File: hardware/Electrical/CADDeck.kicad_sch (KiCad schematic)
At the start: 46 parts, among them J1 Conn_01x05_Socket, J2 Conn_01x05_Pin, J3 Conn_01x04_Pin, J4 Conn_01x04_Socket, J5 Conn_01x10_Socket, J6 Conn_01x10_Pin, Q1 2N2222, SW1 SW_Push, SW10 SW_Push, SW2 SW_Push, SW3 SW_Push, SW4 SW_Push, SW5 SW_Push, SW6 SW_Push, SW7 SW_Push, SW8 SW_Push, SW9 SW_Push, U1 PCF8575PWE4, U3 TTP223, U5 49E Rotate, U6 49E Zoom

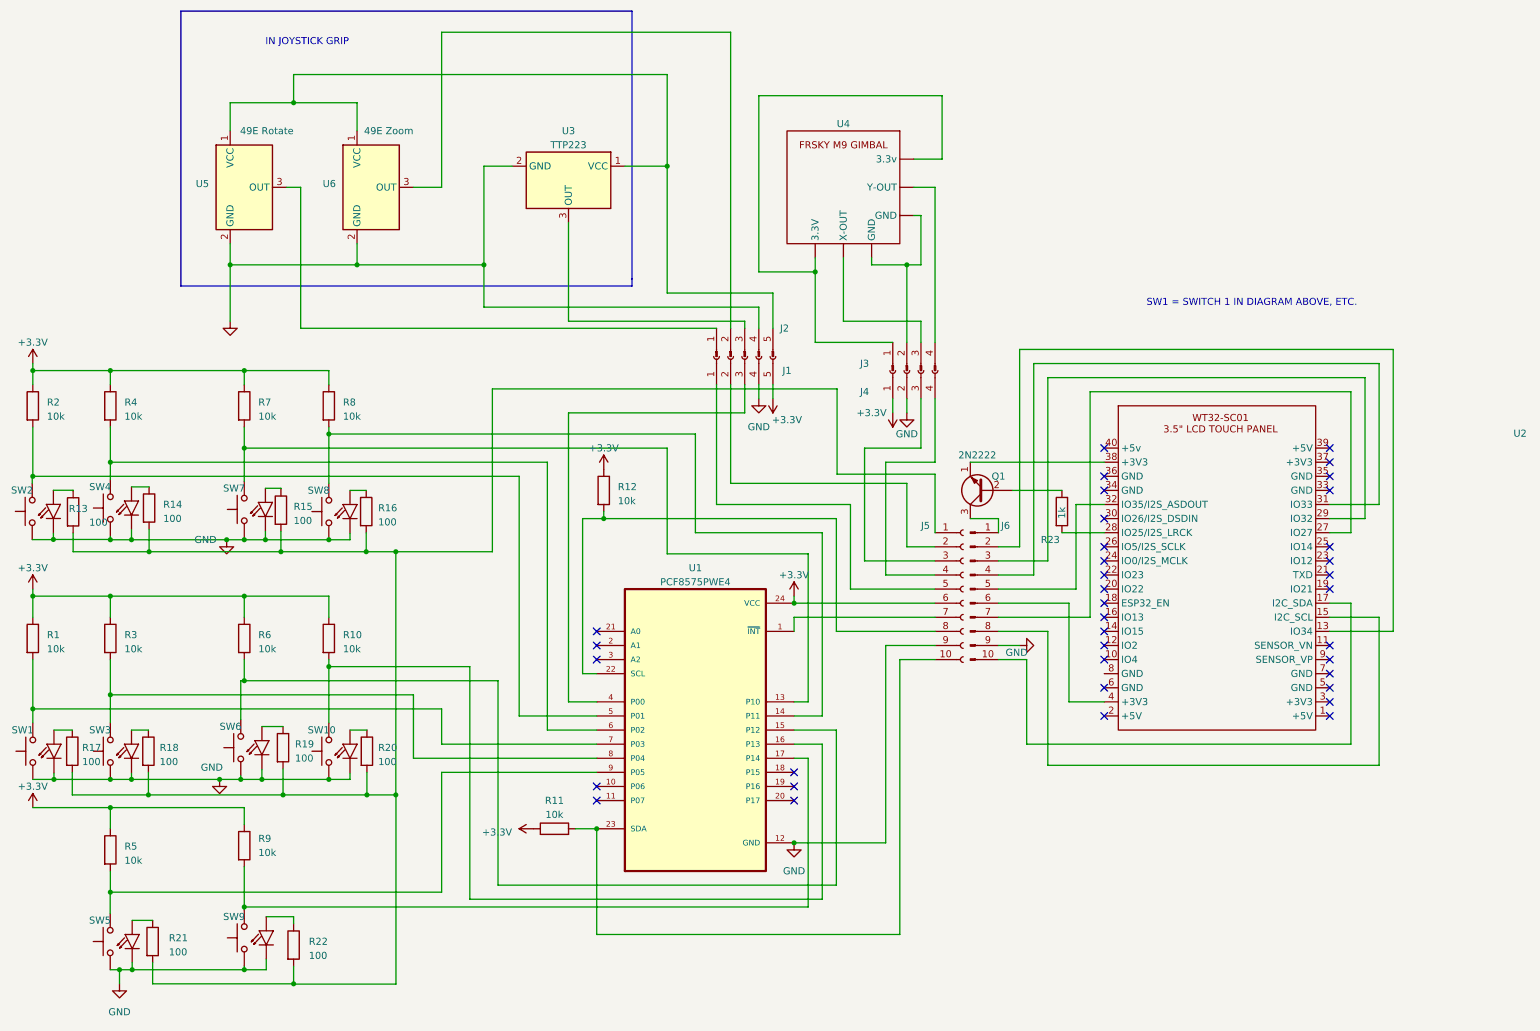
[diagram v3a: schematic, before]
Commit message: Board Transistor eingefügt
Für LED Beleuchtung und Leiterbahnen angepasst.
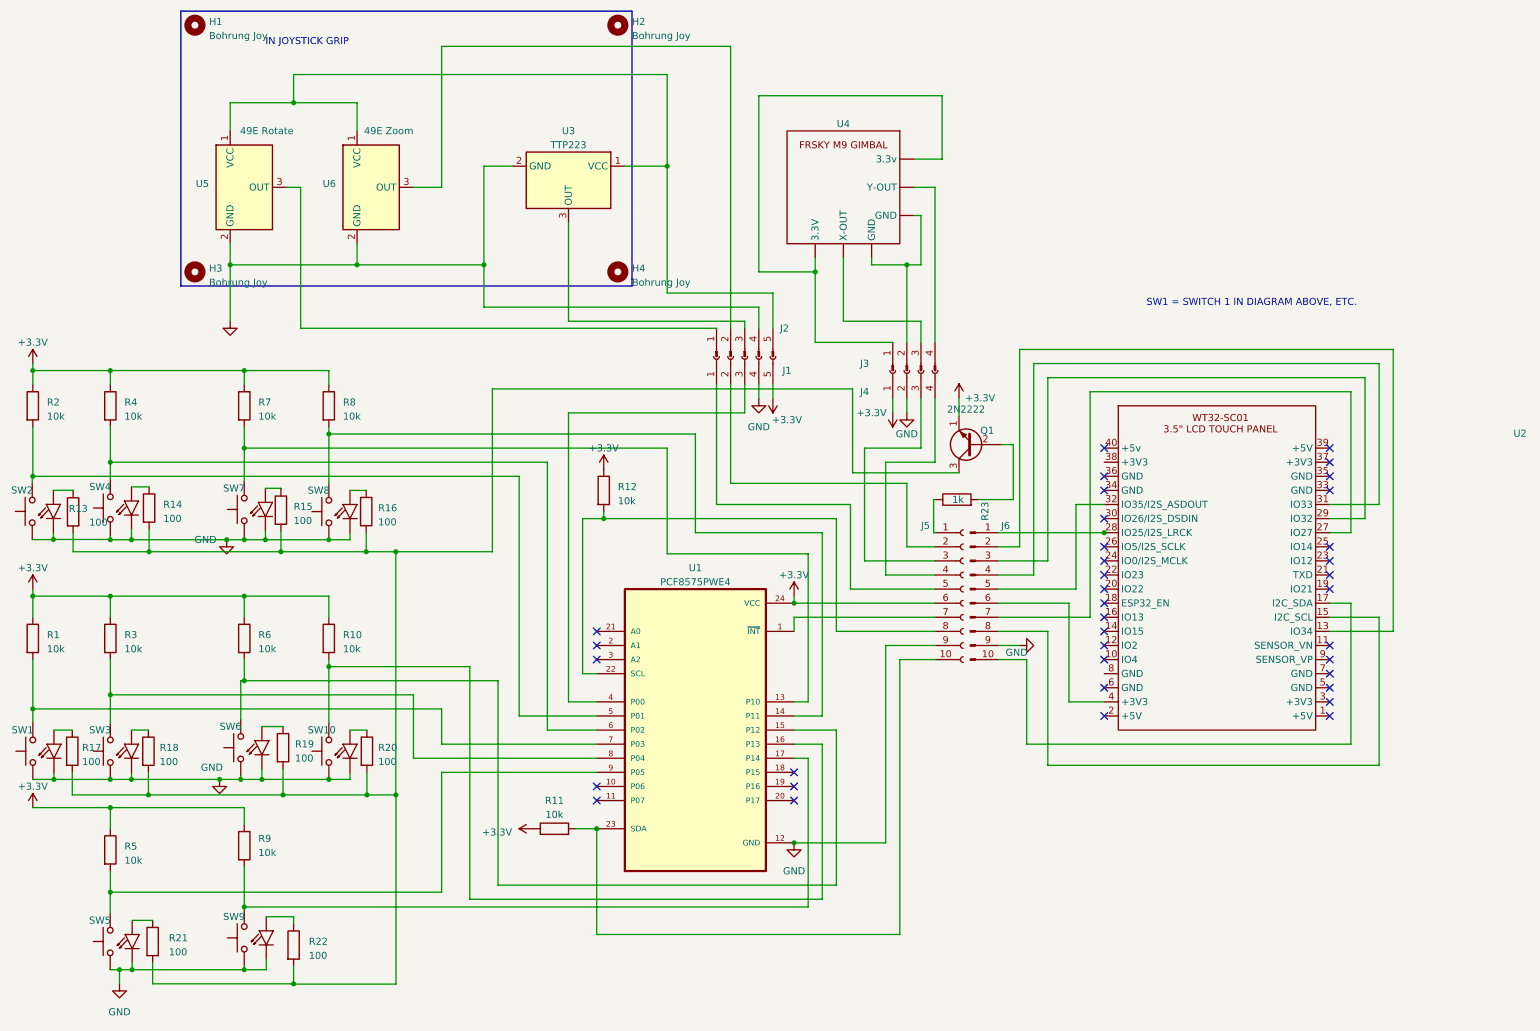
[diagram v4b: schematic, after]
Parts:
- added H1, H2, H3, H4: Bohrung Joy, MountingHole:MountingHole_3.2mm_M3_DIN965, symbol Mechanical:MountingHole
- Q1: footprint Package_TO_SOT_THT:TO-39-3 -> Package_TO_SOT_SMD:TSOT-23
- R23: footprint (none) -> Resistor_SMD:R_0805_2012Metric_Pad1.20x1.40mm_HandSolder
- U3: footprint (none) -> Package_TO_SOT_SMD:TSOT-23
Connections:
- net +3.3V: now also Q1.1 (E)
- net at U2.38 (+3V3): no longer Q1.1 (E)
- net at Q1.2 (B): now also R23.2; no longer R23.1
- net at Q1.3 (C): now also R13.2, R14.2, R15.2, R16.2, R17.2, R18.2, R19.2, R20.2, R21.2, R22.2; no longer J6.1 (Pin_1)
- net at U2.28 (IO25/I2S_LRCK): now also J6.1 (Pin_1); no longer R23.2
- new net: J5.1 (Pin_1), R23.1
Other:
- moved on the sheet: Q1, R23

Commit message: Neue Platine in 3D Modell eingefügt
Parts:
- J1: footprint Connector_JST:JST_EH_B5B-EH-A_1x05_P2.50mm_Vertical -> Connector_JST:JST_EH_S5B-EH_1x05_P2.50mm_Horizontal
- J4: footprint Connector_JST:JST_EH_B4B-EH-A_1x04_P2.50mm_Vertical -> Connector_JST:JST_EH_S4B-EH_1x04_P2.50mm_Horizontal
- J5: footprint Connector_JST:JST_EH_B10B-EH-A_1x10_P2.50mm_Vertical -> Connector_JST:JST_EH_S10B-EH_1x10_P2.50mm_Horizontal
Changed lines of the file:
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@@
       (effects (font (size 1.27 1.27)) hide)
     )
-    (property "Footprint" "Connector_JST:JST_EH_B5B-EH-A_1x05_P2.50mm_Vertical" (at 144.78 78.74 0)
+    (property "Footprint" "Connector_JST:JST_EH_S5B-EH_1x05_P2.50mm_Horizontal" (at 144.78 78.74 0)
       (effects (font (size 1.27 1.27)) hide)
     )
@@
       (effects (font (size 1.27 1.27)) hide)
     )
-    (property "Footprint" "Connector_JST:JST_EH_B4B-EH-A_1x04_P2.50mm_Vertical" (at 173.99 81.28 0)
+    (property "Footprint" "Connector_JST:JST_EH_S4B-EH_1x04_P2.50mm_Horizontal" (at 173.99 81.28 0)
       (effects (font (size 1.27 1.27)) hide)
     )
@@
       (effects (font (size 1.27 1.27)) (justify left) hide)
     )
-    (property "Footprint" "Connector_JST:JST_EH_B10B-EH-A_1x10_P2.50mm_Vertical" (at 184.15 120.65 0)
-      (effects (font (size 1.27 1.27)) hide)
-    )
+    (property "Footprint" "Connector_JST:JST_EH_S10B-EH_1x10_P2.50mm_Horizontal" (at 184.15 120.65 0)
+      (effects (font (size 1.27 1.27)) hide)
+    )

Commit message: Kleine Korrekturen
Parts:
- removed H1, H2, H3, H4: Bohrung Joy, MountingHole:MountingHole_3.2mm_M3_DIN965, symbol Mechanical:MountingHole
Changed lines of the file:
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@@
-    )
-  )
-  (symbol (lib_id "Mechanical:MountingHole") (at 45.72 19.05 0) (unit 1)
-    (in_bom yes) (on_board yes) (dnp no) (fields_autoplaced)
-    (property "Reference" "H1" (at 48.26 18.415 0)
-      (effects (font (size 1.27 1.27)) (justify left))
-    )
-    (property "Value" "Bohrung Joy" (at 48.26 20.955 0)
-      (effects (font (size 1.27 1.27)) (justify left))
-    )
-    (property "Footprint" "MountingHole:MountingHole_3.2mm_M3_DIN965" (at 45.72 19.05 0)
-      (effects (font (size 1.27 1.27)) hide)
-    )
-    (property "Datasheet" "~" (at 45.72 19.05 0)
-      (effects (font (size 1.27 1.27)) hide)
-    )
-    (instances
-      (project "CADDeck"
-        (path "/35ea3785-d2ac-411c-b2c0-fb3fbf77b703"
-          (reference "H1") (unit 1)
-        )
-      )
     )
   )
@@
         (path "/35ea3785-d2ac-411c-b2c0-fb3fbf77b703"
           (reference "R13") (unit 1)
-        )
-      )
-    )
-  )
-  (symbol (lib_id "Mechanical:MountingHole") (at 121.92 19.05 0) (unit 1)
-    (in_bom yes) (on_board yes) (dnp no) (fields_autoplaced)
-    (property "Reference" "H2" (at 124.46 18.415 0)
-      (effects (font (size 1.27 1.27)) (justify left))
-    )
-    (property "Value" "Bohrung Joy" (at 124.46 20.955 0)
-      (effects (font (size 1.27 1.27)) (justify left))
-    )
-    (property "Footprint" "MountingHole:MountingHole_3.2mm_M3_DIN965" (at 121.92 19.05 0)
-      (effects (font (size 1.27 1.27)) hide)
-    )
-    (property "Datasheet" "~" (at 121.92 19.05 0)
-      (effects (font (size 1.27 1.27)) hide)
-    )
-    (instances
-      (project "CADDeck"
-        (path "/35ea3785-d2ac-411c-b2c0-fb3fbf77b703"
-          (reference "H2") (unit 1)
         )
       )
@@
         (path "/35ea3785-d2ac-411c-b2c0-fb3fbf77b703"
           (reference "#PWR07") (unit 1)
-        )
-      )
-    )
-  )
-  (symbol (lib_id "Mechanical:MountingHole") (at 121.92 63.5 0) (unit 1)
-    (in_bom yes) (on_board yes) (dnp no) (fields_autoplaced)
-    (property "Reference" "H4" (at 124.46 62.865 0)
-      (effects (font (size 1.27 1.27)) (justify left))
-    )
-    (property "Value" "Bohrung Joy" (at 124.46 65.405 0)
-      (effects (font (size 1.27 1.27)) (justify left))
-    )
-    (property "Footprint" "MountingHole:MountingHole_3.2mm_M3_DIN965" (at 121.92 63.5 0)
-      (effects (font (size 1.27 1.27)) hide)
-    )
-    (property "Datasheet" "~" (at 121.92 63.5 0)
-      (effects (font (size 1.27 1.27)) hide)
-    )
-    (instances
-      (project "CADDeck"
-        (path "/35ea3785-d2ac-411c-b2c0-fb3fbf77b703"
-          (reference "H4") (unit 1)
         )
       )
@@
         )
       )
-    )
-  )
-  (symbol (lib_id "Mechanical:MountingHole") (at 45.72 63.5 0) (unit 1)
-    (in_bom yes) (on_board yes) (dnp no) (fields_autoplaced)
-    (property "Reference" "H3" (at 48.26 62.865 0)
-      (effects (font (size 1.27 1.27)) (justify left))
-    )
-    (property "Value" "Bohrung Joy" (at 48.26 65.405 0)
-      (effects (font (size 1.27 1.27)) (justify left))
-    )
-    (property "Footprint" "MountingHole:MountingHole_3.2mm_M3_DIN965" (at 45.72 63.5 0)
-      (effects (font (size 1.27 1.27)) hide)
-    )
-    (property "Datasheet" "~" (at 45.72 63.5 0)
-      (effects (font (size 1.27 1.27)) hide)
-    )
-    (instances
-      (project "CADDeck"
-        (path "/35ea3785-d2ac-411c-b2c0-fb3fbf77b703"
-          (reference "H3") (unit 1)
-        )
-      )

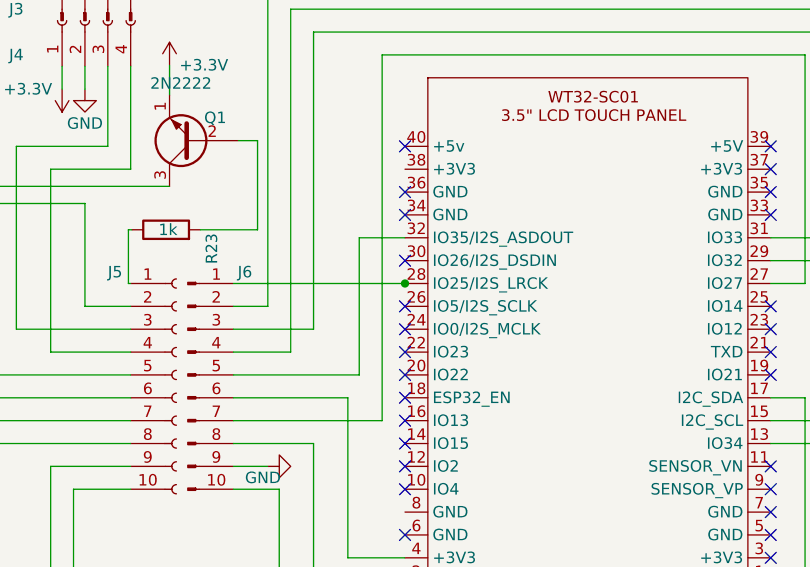
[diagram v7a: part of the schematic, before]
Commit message: Footprints geändert
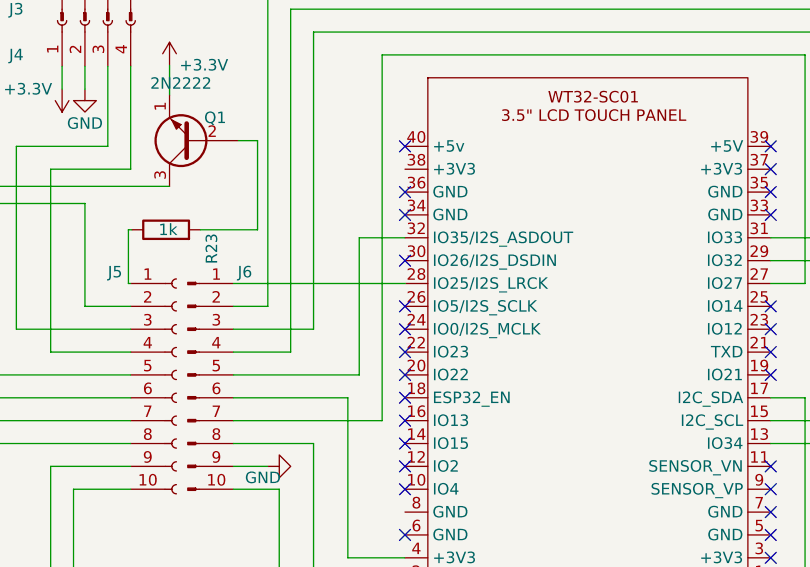
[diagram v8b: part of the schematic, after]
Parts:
- J1: footprint Connector_JST:JST_EH_S5B-EH_1x05_P2.50mm_Horizontal -> Connector_JST:JST_EH_B5B-EH-A_1x05_P2.50mm_Vertical
- J4: footprint Connector_JST:JST_EH_S4B-EH_1x04_P2.50mm_Horizontal -> Connector_JST:JST_EH_B4B-EH-A_1x04_P2.50mm_Vertical
- J5: footprint Connector_JST:JST_EH_S10B-EH_1x10_P2.50mm_Horizontal -> Connector_JST:JST_EH_B10B-EH-A_1x10_P2.50mm_Vertical
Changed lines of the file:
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@@
   (junction (at 54.61 111.76) (diameter 0) (color 0 0 0 0)
   )
-  (junction (at 209.55 110.49) (diameter 0) (color 0 0 0 0)
-  )
   (junction (at 16.51 142.24) (diameter 0) (color 0 0 0 0)
   )
@@
     (stroke (width 0) (type default))
   )
+  (wire (pts (xy 190.5 110.49) (xy 209.55 110.49))
+    (stroke (width 0) (type default))
+  )
   (wire (pts (xy 34.29 154.94) (xy 50.165 154.94))
     (stroke (width 0) (type default))
@@
     (stroke (width 0) (type default))
   )
-  (wire (pts (xy 190.5 110.49) (xy 209.55 110.49))
-    (stroke (width 0) (type default))
-  )
   (wire (pts (xy 193.167 94.615) (xy 193.167 104.521))
     (stroke (width 0) (type default))
@@
     (stroke (width 0) (type default))
   )
-  (wire (pts (xy 209.677 110.49) (xy 209.55 110.49))
-    (stroke (width 0) (type default))
-  )
   (wire (pts (xy 90.17 142.24) (xy 90.17 148.59))
     (stroke (width 0) (type default))
@@
       (effects (font (size 1.27 1.27)) hide)
     )
-    (property "Footprint" "Connector_JST:JST_EH_S5B-EH_1x05_P2.50mm_Horizontal" (at 144.78 78.74 0)
+    (property "Footprint" "Connector_JST:JST_EH_B5B-EH-A_1x05_P2.50mm_Vertical" (at 144.78 78.74 0)
       (effects (font (size 1.27 1.27)) hide)
     )
@@
       (effects (font (size 1.27 1.27)) hide)
     )
-    (property "Footprint" "Connector_JST:JST_EH_S4B-EH_1x04_P2.50mm_Horizontal" (at 173.99 81.28 0)
+    (property "Footprint" "Connector_JST:JST_EH_B4B-EH-A_1x04_P2.50mm_Vertical" (at 173.99 81.28 0)
       (effects (font (size 1.27 1.27)) hide)
     )
@@
       (effects (font (size 1.27 1.27)) (justify left) hide)
     )
-    (property "Footprint" "Connector_JST:JST_EH_S10B-EH_1x10_P2.50mm_Horizontal" (at 184.15 120.65 0)
+    (property "Footprint" "Connector_JST:JST_EH_B10B-EH-A_1x10_P2.50mm_Vertical" (at 184.15 120.65 0)
       (effects (font (size 1.27 1.27)) hide)
     )
